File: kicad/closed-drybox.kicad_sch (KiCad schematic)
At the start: 23 parts, among them J1 Power_Jack, M1 Fan, M2 Fan, Q1 AO3400A, Q2 AO3400A, Q3 AO3400A, Q4 AO3400A, Q5 AO3400A, Q6 AO3400A, Q7 AO3400A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

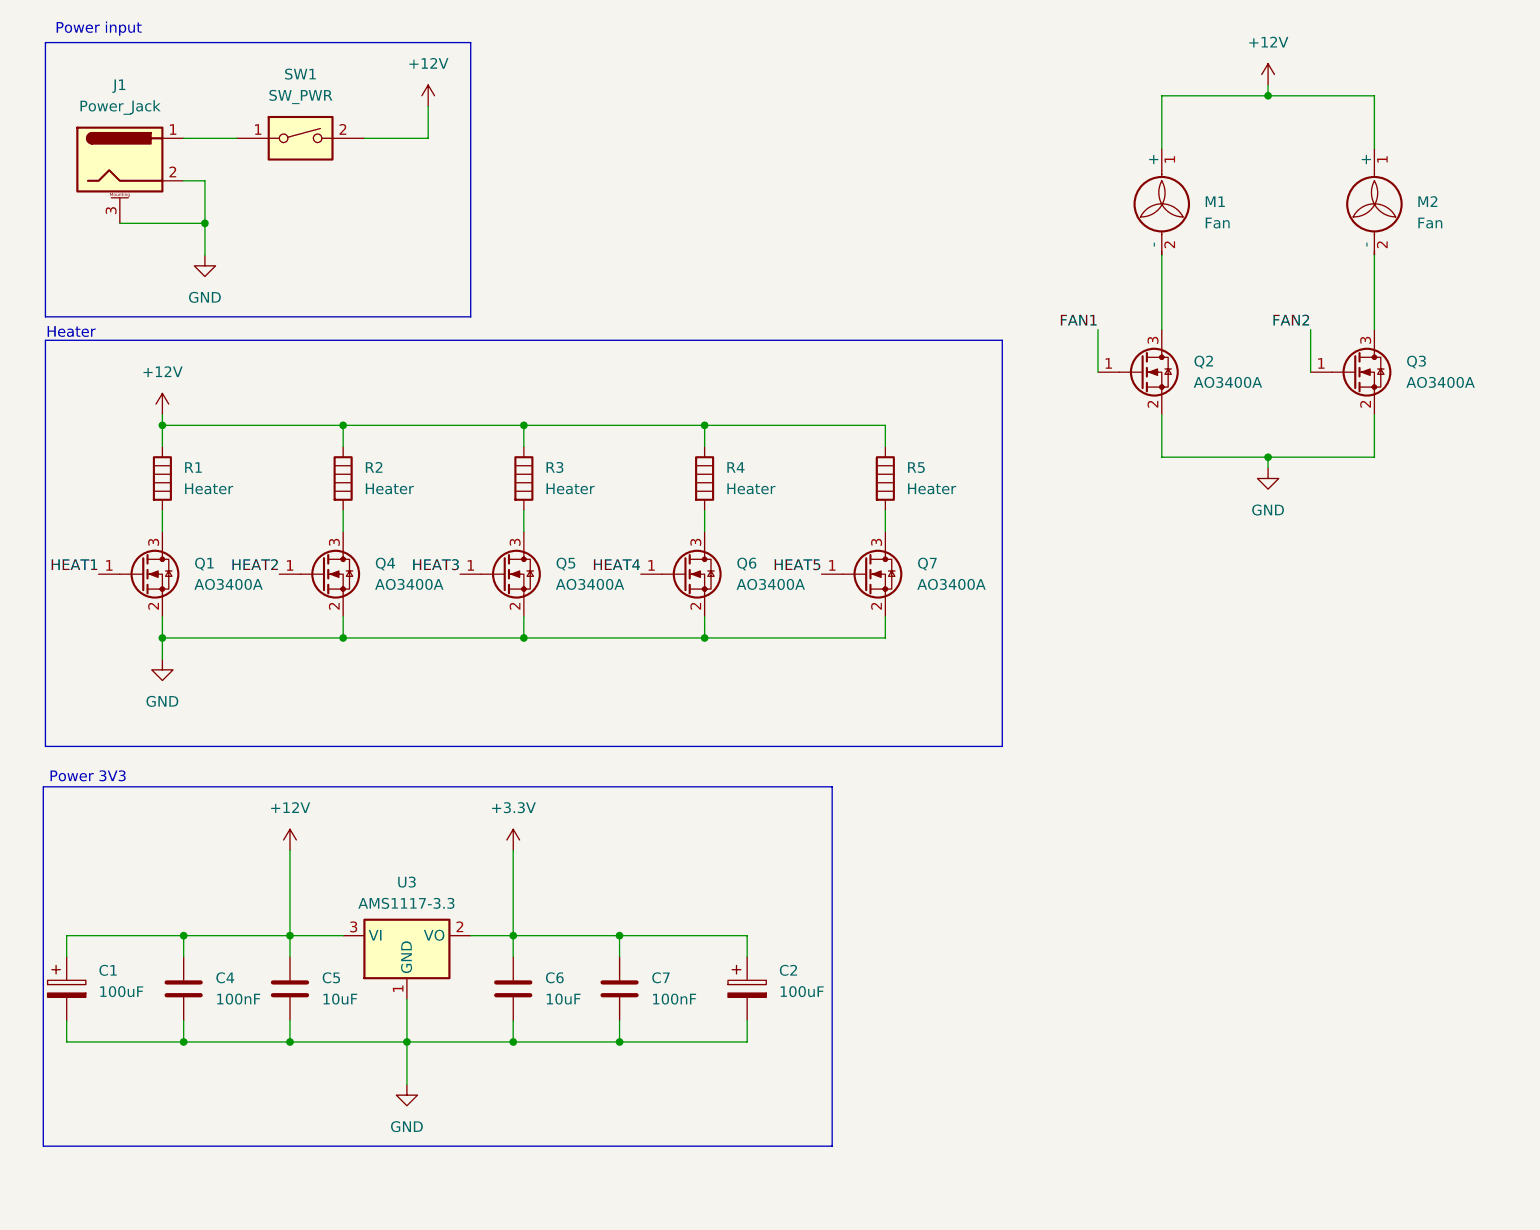
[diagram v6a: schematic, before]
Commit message: add esp32, add boxes
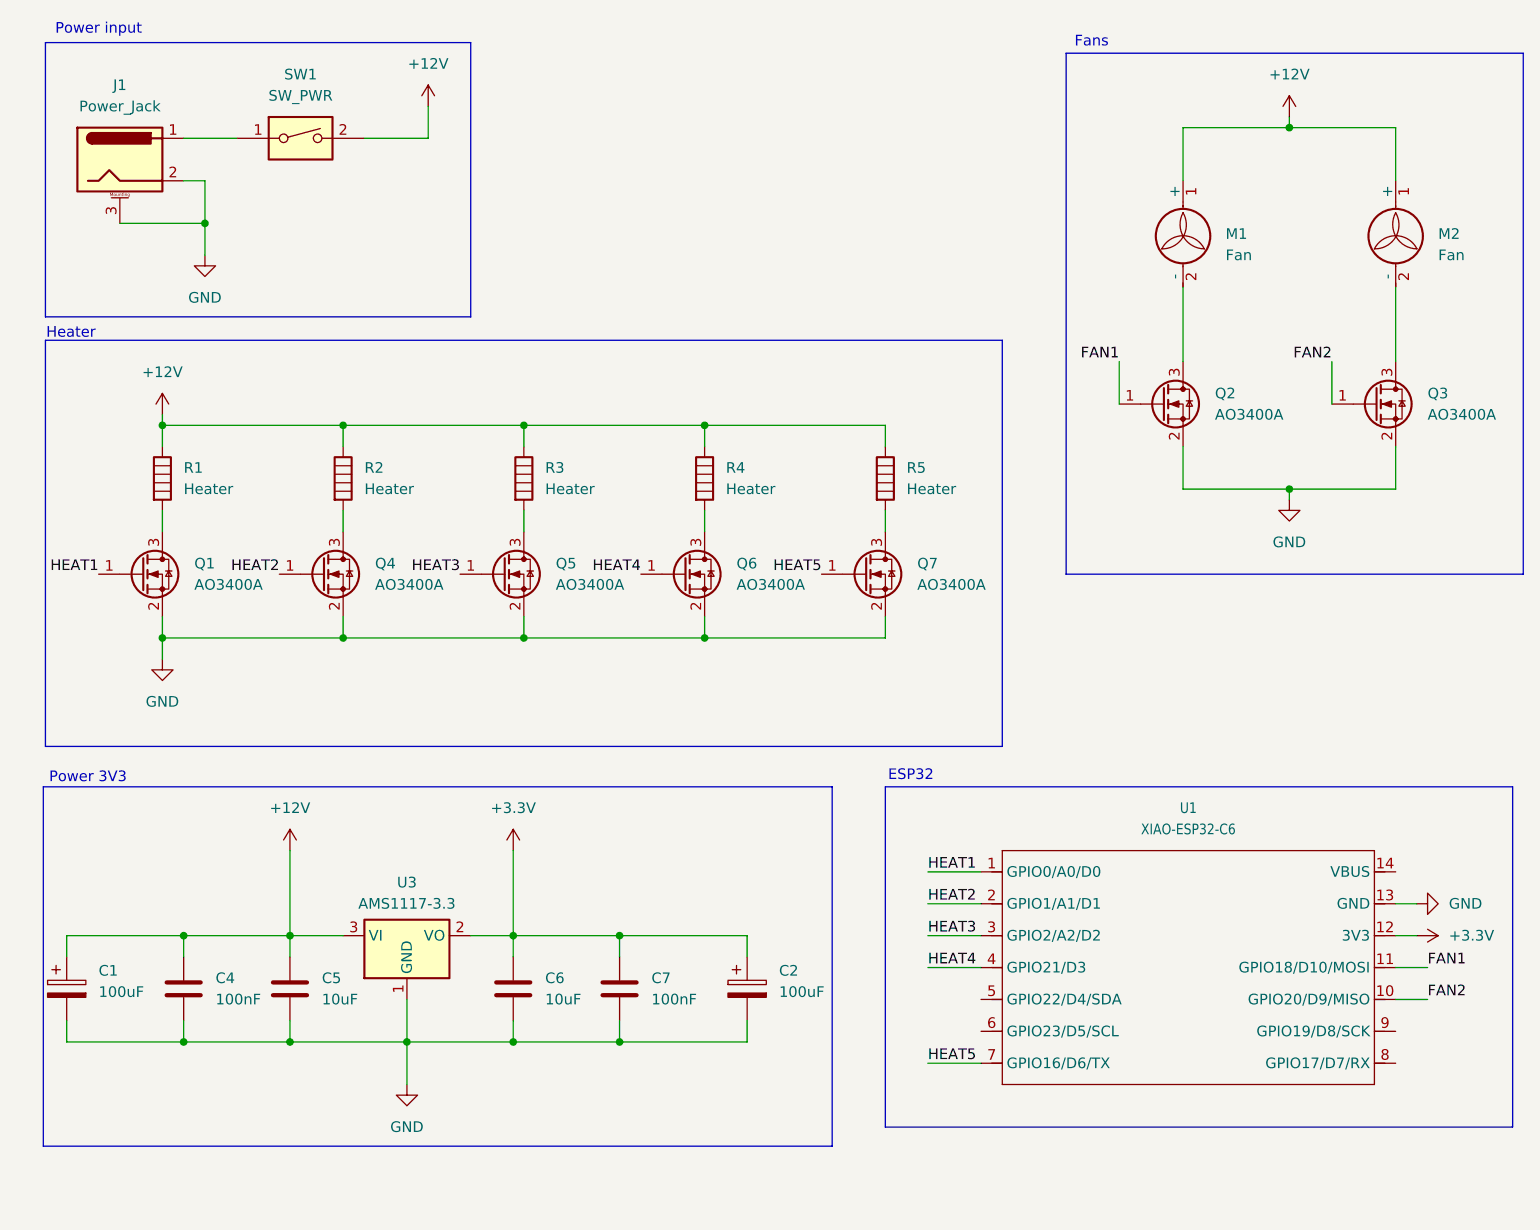
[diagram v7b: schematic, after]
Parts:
- added U1: XIAO-ESP32-C6, CustomLibrary:XIAO-ESP32C6-DIP, symbol CustomLibary:XIAO_ESP32-C6-DIP
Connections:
- net +3.3V: now also U1.12 (3V3)
- net FAN1: now also U1.11 (GPIO18/D10/MOSI)
- net FAN2: now also U1.10 (GPIO20/D9/MISO)
- net GND: now also U1.13 (GND)
- net HEAT1: now also U1.1 (GPIO0/A0/D0)
- net HEAT2: now also U1.2 (GPIO1/A1/D1)
- net HEAT3: now also U1.3 (GPIO2/A2/D2)
- net HEAT4: now also U1.4 (GPIO21/D3)
- net HEAT5: now also U1.7 (GPIO16/D6/TX)
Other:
- note added: "ESP32"
- note added: "Fans"
- moved on the sheet: M1, M2, Q2, Q3

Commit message: add power messurement
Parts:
- added JP?: SolderJumper_2_Open, Jumper:SolderJumper-2_P1.3mm_Open_RoundedPad1.0x1.5mm, symbol Jumper:SolderJumper_2_Open
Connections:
- net +12V: now also JP?.2 (B); no longer SW1.2
- net SDA: now reaches U1.5 (GPIO22/D4/SDA)
- net SCL: now reaches U1.6 (GPIO23/D5/SCL)
- new net power measurement/IN: JP?.1 (A), SW1.2
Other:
- added sheet power measurement (INA219AIDCNR.kicad_sch)
